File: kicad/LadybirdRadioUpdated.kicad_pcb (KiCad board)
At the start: 2 copper layers, 133.8 x 93.1 mm, 32 parts, among them J1 Conn_01x02_Pin, J2 Conn_01x02_Pin, J3 Conn_01x02_Pin, J4 Conn_01x03_Pin, Q1 BC547, Q2 BC337, Q3 BC337, T1 Transformer_P631T

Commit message: Updated README
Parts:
- L2: footprint Inductor_THT:L_Axial_L12.8mm_D5.8mm_P25.40mm_Horizontal_Fastron_HBCC -> ACRM:L_Axial_L12.8mm_D5.8mm_P25.40mm_Horizontal_Radial_D9.5mm_P5.0mm
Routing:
- net Net-(Q1-C): track 69.3 -> 79.5 mm
- net Net-(C4-Pad1): track 25.0 -> 35.2 mm
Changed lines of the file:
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@@
 		)
 	)
-	(footprint "Inductor_THT:L_Axial_L12.8mm_D5.8mm_P25.40mm_Horizontal_Fastron_HBCC"
+	(footprint "ACRM:L_Axial_L12.8mm_D5.8mm_P25.40mm_Horizontal_Radial_D9.5mm_P5.0mm"
 		(layer "F.Cu")
 		(at 70 58.6 -90)
@@
 		(tags "Inductor Axial series Axial Horizontal pin pitch 25.4mm  length 12.8mm diameter 5.8mm Fastron HBCC")
 		(property "Reference" "L2"
-			(at 7 4.3 0)
+			(at 13.15 -6.35 270)
 			(layer "F.SilkS")
 			(effects
@@
 		)
 		(property "Value" "2.2mH"
-			(at 18.6 5.7 180)
-			(layer "F.SilkS")
+			(at 12.7 4.02 270)
+			(layer "F.Fab")
 			(effects
 				(font
@@
 			(layer "F.SilkS")
 		)
+		(fp_circle
+			(center 12.7 -0.05)
+			(end 17.57 -0.05)
+			(stroke
+				(width 0.12)
+				(type solid)
+			)
+			(fill no)
+			(layer "F.SilkS")
+		)
 		(fp_line
 			(start -1.35 3.15)
@@
 			(layer "F.CrtYd")
 		)
+		(fp_circle
+			(center 12.7 -0.05)
+			(end 17.7 -0.05)
+			(stroke
+				(width 0.05)
+				(type solid)
+			)
+			(fill no)
+			(layer "F.CrtYd")
+		)
 		(fp_line
 			(start 6.3 2.9)
@@
 			(layer "F.Fab")
 		)
+		(fp_circle
+			(center 12.7 -0.05)
+			(end 17.45 -0.05)
+			(stroke
+				(width 0.1)
+				(type solid)
+			)
+			(fill no)
+			(layer "F.Fab")
+		)
+		(fp_text user "${REFERENCE}"
+			(at 12.7 0 270)
+			(layer "F.Fab")
+			(effects
+				(font
+					(size 1 1)
+					(thickness 0.15)
+				)
+			)
+		)
 		(fp_text user "${REFERENCE}"
-			(at 12.7 0 90)
+			(at 12.7 -0.05 270)
 			(layer "F.Fab")
 			(effects
@@
 			(pintype "passive")
 		)
+		(pad "1" thru_hole circle
+			(at 10.2 -0.05 270)
+			(size 2.6 2.6)
+			(drill 1.3)
+			(layers "*.Cu" "*.Mask")
+			(remove_unused_layers no)
+			(net 5 "Net-(C4-Pad1)")
+			(pinfunction "1")
+			(pintype "passive")
+		)
+		(pad "2" thru_hole circle
+			(at 15.2 -0.05 270)
+			(size 2.6 2.6)
+			(drill 1.3)
+			(layers "*.Cu" "*.Mask")
+			(remove_unused_layers no)
+			(net 1 "Net-(Q1-C)")
+			(pinfunction "2")
+			(pintype "passive")
+		)
 		(pad "2" thru_hole oval
 			(at 25.4 0 270)
@@
 	)
 	(segment
+		(start 70 73.85)
+		(end 70.05 73.8)
+		(width 1)
+		(layer "B.Cu")
+		(net 1)
+	)
+	(segment
 		(start 61 49.7)
 		(end 54.3 43)
@@
 	(segment
 		(start 70 84)
+		(end 70 73.85)
+		(width 1)
+		(layer "B.Cu")
+		(net 1)
+	)
+	(segment
+		(start 70 84)
 		(end 70 89.520736)
 		(width 1)
@@
 	)
 	(segment
+		(start 70 58.6)
+		(end 70 68.75)
+		(width 1)
+		(layer "B.Cu")
+		(net 5)
+	)
+	(segment
 		(start 80.5 53)
 		(end 70 53)
 		(width 1)
 		(layer "B.Cu")
+		(net 5)
+	)
+	(segment
+		(start 70 68.75)
+		(end 70.05 68.8)
+		(width 1)
+		(layer "B.Cu")

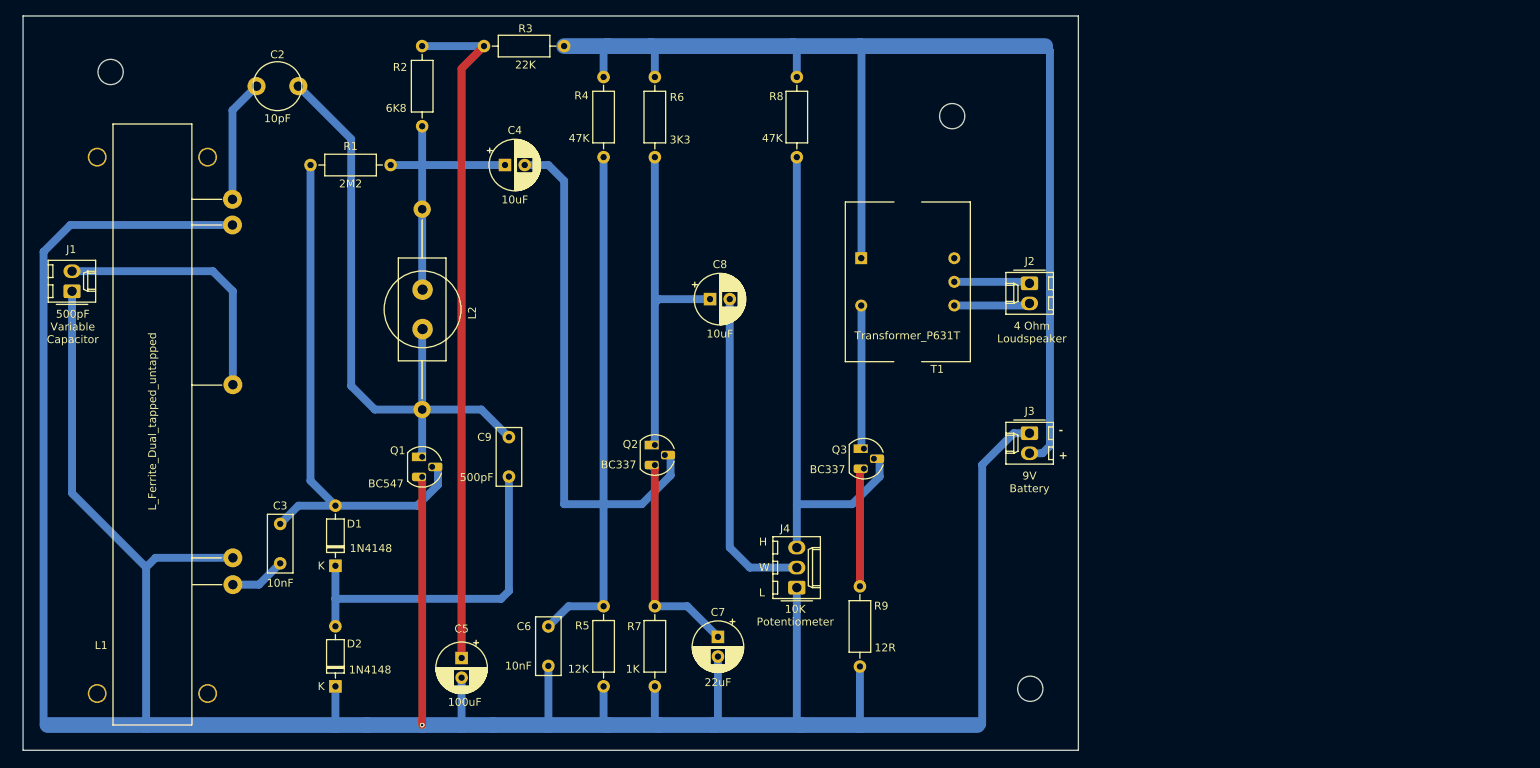
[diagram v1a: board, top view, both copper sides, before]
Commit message: Added options for crystal set
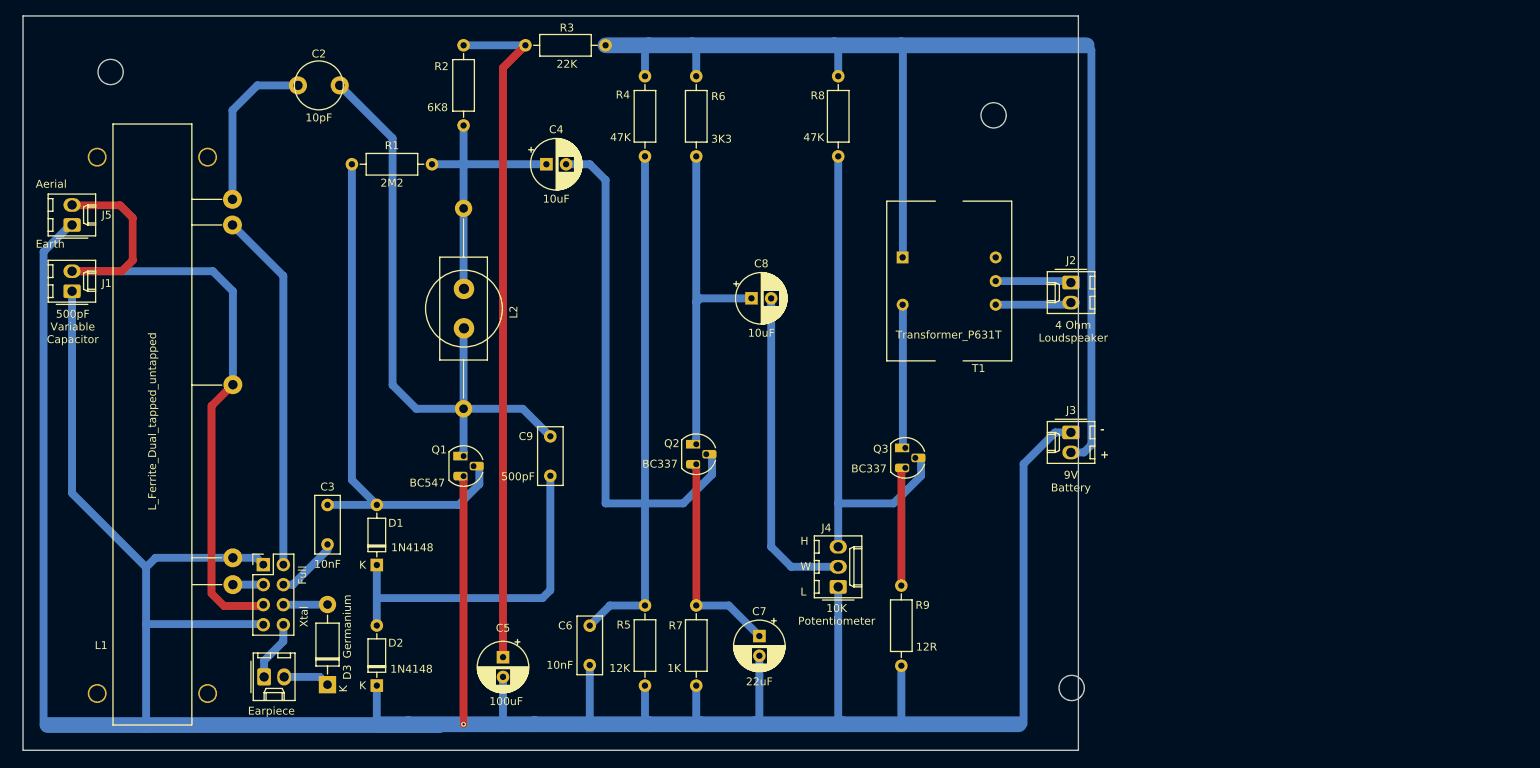
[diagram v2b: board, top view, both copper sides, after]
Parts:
- added D3: Germanium, Diode_THT:D_DO-41_SOD81_P10.16mm_Horizontal, F.Cu at (58.0, 118.9)
- added J5: Conn_01x02_Pin, Connector_Molex:Molex_KK-254_AE-6410-02A_1x02_P2.54mm_Vertical, F.Cu at (25.6, 60.6)
- added J8: Conn_02x04_Odd_Even, Connector_PinHeader_2.54mm:PinHeader_2x04_P2.54mm_Vertical, F.Cu at (49.9, 103.7)
- added J9: Conn_01x02_Pin, Connector_Molex:Molex_KK-254_AE-6410-02A_1x02_P2.54mm_Vertical, F.Cu at (50.0, 117.9)
- moved C3 6.46 mm to (58.0, 101.1)
- moved C2 5.25 mm to (56.9, 42.9)
- moved C4 5.25 mm to (85.8, 52.9)
- moved C5 5.25 mm to (80.2, 115.4)
- moved C6 5.25 mm to (91.2, 111.4)
- moved C7 5.25 mm to (112.8, 112.7)
- moved C8 5.25 mm to (111.8, 69.9)
- moved C9 5.25 mm to (86.2, 87.4)
- moved D1 5.25 mm to (64.2, 103.7)
- moved D2 5.25 mm to (64.2, 119.0)
- moved J2 5.25 mm to (152.2, 67.9)
- moved J3 5.25 mm to (152.2, 86.9)
- moved J4 5.25 mm to (122.8, 106.5)
- moved L2 5.25 mm to (75.2, 58.5)
- moved Q1 5.25 mm to (75.2, 89.9)
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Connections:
- C3 pad 1: Net-(C3-Pad1) -> Net-(J8-Pin_4)
- L1 pad 1: Net-(C3-Pad1) -> Net-(J8-Pin_3)
- L1 pad 4: GND -> Net-(J8-Pin_2)
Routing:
- net Net-(J1-Pin_2): track 33.3 -> 90.2 mm
- net Net-(J8-Pin_2): track 0.00 -> 45.7 mm
- net GND: track 408.2 -> 419.9 mm
- net Net-(J8-Pin_4): track 0.00 -> 8.12 mm
- net Net-(J8-Pin_8): track 0.00 -> 7.63 mm
- net Net-(C3-Pad1): track 7.12 -> 0.00 mm
- net Net-(D3-K): track 0.00 -> 5.91 mm
- net Net-(D3-A): track 0.00 -> 5.61 mm
- net Net-(C2-Pad1): track 15.6 -> 20.9 mm
- net Net-(J8-Pin_3): track 0.00 -> 3.30 mm
- net Net-(D1-A): track 68.8 -> 67.1 mm
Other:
- board text added: "Aerial"
- board text added: "Earpiece"
- board text added: "Earth"
- board text added: "Full"
- board text added: "Xtal"

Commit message: PCB done but needs annotating
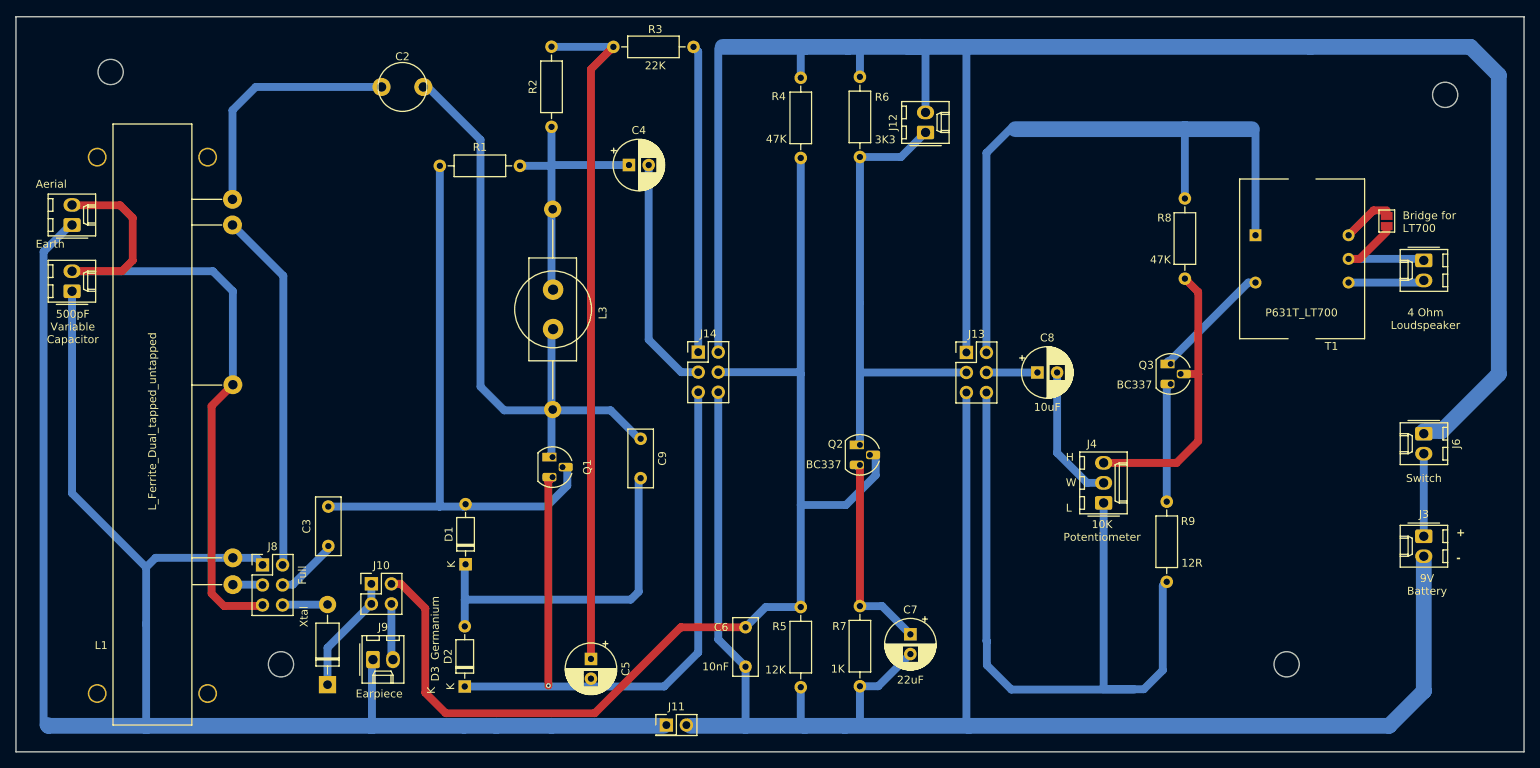
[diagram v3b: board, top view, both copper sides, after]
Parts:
- removed L2: 2.2mH, ACRM:L_Axial_L12.8mm_D5.8mm_P25.40mm_Horizontal_Radial_D9.5mm_P5.0mm
- added J10: Conn_02x02_Odd_Even, Connector_PinHeader_2.54mm:PinHeader_2x02_P2.54mm_Vertical, F.Cu at (63.6, 106.1)
- added J11: Conn_02x01, Connector_PinHeader_2.54mm:PinHeader_2x01_P2.54mm_Vertical, F.Cu at (101.0, 124.0)
- added J12: Conn_01x02_Pin, Connector_Molex:Molex_KK-254_AE-6410-02A_1x02_P2.54mm_Vertical, F.Cu at (133.8, 48.9)
- added J13: Conn_02x03_Odd_Even, Connector_PinHeader_2.54mm:PinHeader_2x03_P2.54mm_Vertical, F.Cu at (139.0, 76.8)
- added J14: Conn_02x03_Odd_Even, Connector_PinHeader_2.54mm:PinHeader_2x03_P2.54mm_Vertical, F.Cu at (105.0, 76.7)
- added J6: Conn_01x02_Pin, Connector_Molex:Molex_KK-254_AE-6410-02A_1x02_P2.54mm_Vertical, F.Cu at (197.0, 87.1)
- added JP1: SolderJumper_2_Open, Jumper:SolderJumper-2_P1.3mm_Open_Pad1.0x1.5mm, F.Cu at (192.3, 60.1)
- added L3: 2.2mH, ACRM:L_Axial_L12.8mm_D5.8mm_P25.40mm_Horizontal_Radial_D9.5mm_P5.0mm, F.Cu at (86.5, 58.6)
- added REF**: MountingHole_3.2mm_M3, MountingHole:MountingHole_3.2mm_M3, F.Cu at (52.1, 116.3)
- J1: value Conn_01x02_Pin -> VCap
- J5: value Conn_01x02_Pin -> A/E
- J8: value Conn_02x04_Odd_Even -> Conn_02x03_Odd_Even; footprint Connector_PinHeader_2.54mm:PinHeader_2x04_P2.54mm_Vertical -> Connector_PinHeader_2.54mm:PinHeader_2x03_P2.54mm_Vertical
- T1: value Transformer_P631T -> P631T_LT700
- moved REF** 57.3 mm to (199.7, 44.1)
- moved J3 46.6 mm to (197.0, 100.1)
- moved R8 46.6 mm to (166.7, 57.2)
- moved J2 44.8 mm to (197.0, 65.1)
- moved T1 44.8 mm to (188.4, 60.1)
- moved C8 37.4 mm to (148.0, 79.3)
- moved J4 35.3 mm to (156.4, 95.8)
- moved Q3 35.3 mm to (164.9, 78.2)
- moved R9 35.3 mm to (164.4, 95.7)
- moved REF** 27.4 mm to (179.6, 116.3)
- moved Q2 20.8 mm to (125.5, 88.5)
- moved R6 20.8 mm to (125.5, 41.8)
- moved R7 20.8 mm to (125.5, 108.9)
- moved C6 19.8 mm to (111.0, 111.6)
- moved R4 19.8 mm to (118.0, 41.9)
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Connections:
- C4 pad 2: Net-(Q2-B) -> Net-(J14-Pin_3)
- C5 pad 2: GND -> Net-(D2-K)
- C6 pad 1: Net-(Q2-B) -> Net-(J10-Pin_2)
- C6 pad 2: GND -> /GND2
- C7 pad 2: GND -> /GND2
- C8 pad 1: Net-(Q2-C) -> Net-(J13-Pin_4)
- D2 pad 1: GND -> Net-(D2-K)
- J3 pad 1: GND -> Net-(J3-Pin_1)
- J3 pad 2: Net-(J3-Pin_2) -> /GND2
- J4 pad 1: GND -> Net-(J13-Pin_6)
- J9 pad 1: Net-(J8-Pin_8) -> GND
- J9 pad 2: Net-(D3-K) -> Net-(J10-Pin_4)
- Q1 pad 3: GND -> Net-(D2-K)
- Q2 pad 1: Net-(Q2-C) -> Net-(J12-Pin_1)
- Q2 pad 2: Net-(Q2-B) -> Net-(J10-Pin_2)
- R3 pad 1: Net-(J3-Pin_2) -> Net-(J14-Pin_1)
- R4 pad 1: Net-(J3-Pin_2) -> /+ve
- R4 pad 2: Net-(Q2-B) -> Net-(J10-Pin_2)
- R5 pad 1: Net-(Q2-B) -> Net-(J10-Pin_2)
- R5 pad 2: GND -> /GND2
- R6 pad 1: Net-(J3-Pin_2) -> /+ve
- R6 pad 2: Net-(Q2-C) -> Net-(J12-Pin_1)
- R7 pad 2: GND -> /GND2
- R8 pad 1: Net-(J3-Pin_2) -> Net-(J13-Pin_2)
- R9 pad 2: GND -> Net-(J13-Pin_6)
- T1 pad 1: Net-(J3-Pin_2) -> Net-(J13-Pin_2)
- T1 pad 5: unconnected-(T1-SB-Pad5) -> Net-(JP1-A)
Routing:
- net /+ve: track 0.00 -> 245.4 mm
- net /GND2: track 0.00 -> 215.3 mm
- net GND: track 419.9 -> 226.0 mm, vias 1 -> 0
- net Net-(J3-Pin_2): track 154.3 -> 0.00 mm
- net Net-(J10-Pin_2): track 0.00 -> 151.4 mm
- net Net-(Q2-B): track 129.2 -> 0.00 mm
- net Net-(J13-Pin_6): track 0.00 -> 98.3 mm
- net Net-(D2-K): track 0.00 -> 91.7 mm, vias 0 -> 1
- net Net-(J13-Pin_2): track 0.00 -> 81.7 mm
- net Net-(J12-Pin_1): track 0.00 -> 59.5 mm
- net Net-(Q2-C): track 43.6 -> 0.00 mm
- net Net-(J14-Pin_1): track 0.00 -> 38.9 mm
- net Net-(J14-Pin_3): track 0.00 -> 30.1 mm
- net Net-(J4-Pin_3): track 63.5 -> 35.9 mm
- net Net-(J4-Pin_2): track 41.1 -> 17.7 mm
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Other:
- board size 133.8 x 93.1 mm -> 191.2 x 93.2 mm
- board text added: "+ -"
- board text added: "Bridge for LT700"
- board text added: "Switch"
- board text removed: "- +"

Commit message: Added board annotation and expanded readme
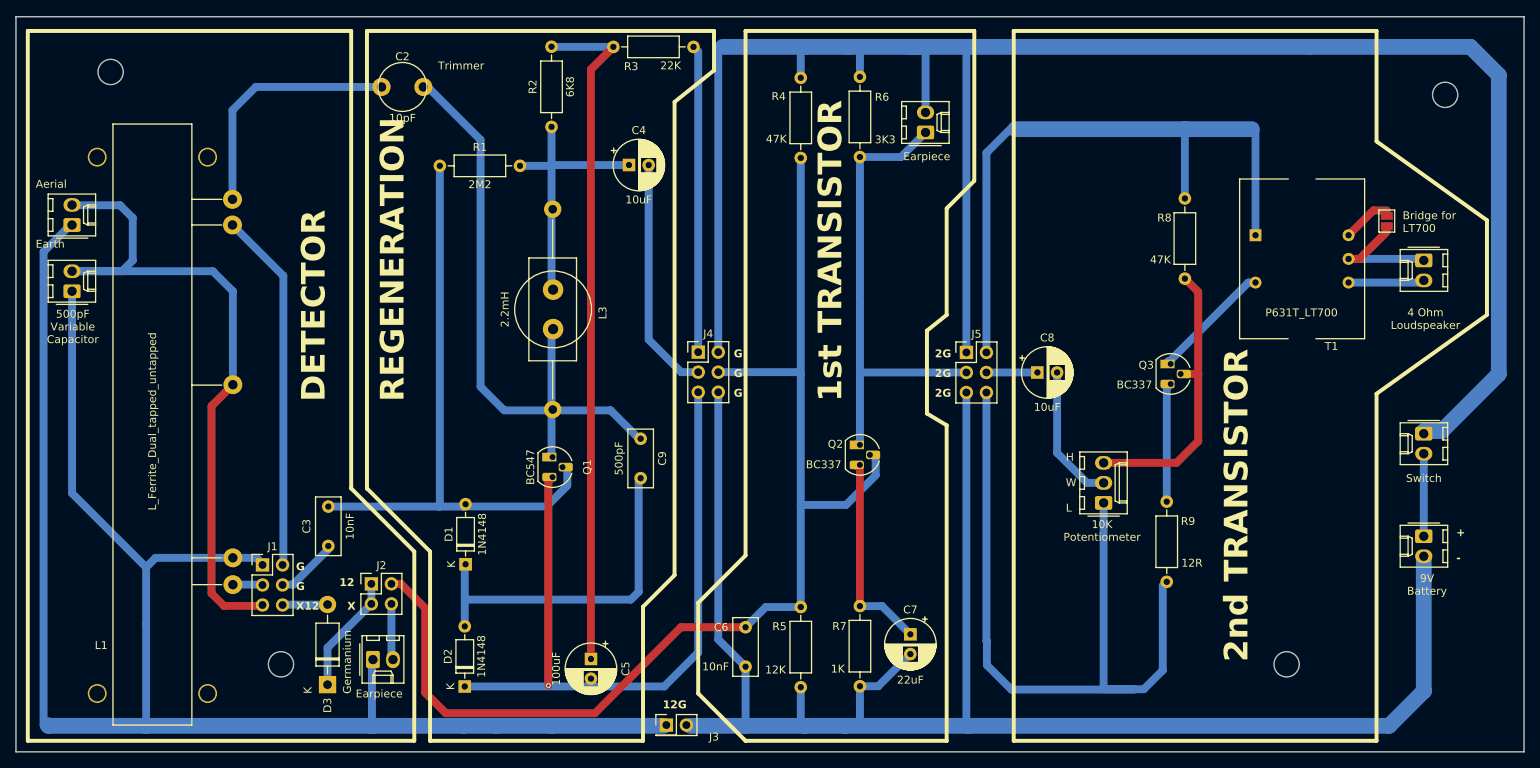
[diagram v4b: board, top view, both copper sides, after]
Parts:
- renumbered J8 to J1, J5 to J11, J1 to J12, J9 to J13, J12 to J14, J4 to J15, J2 to J16, J3 to J17, J6 to J18, J10 to J2, J11 to J3, J14 to J4, J13 to J5
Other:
- board text added: "12"
- board text added: "12G"
- board text added: "1st TRANSISTOR"
- board text added: "2G"
- board text added: "2nd TRANSISTOR"
- board text added: "DETECTOR"
- board text added: "G"
- board text added: "REGENERATION"
- board text added: "Trimmer"
- board text added: "X"
- board text added: "X12"
- board text removed: "Full"
- board text removed: "Xtal"
